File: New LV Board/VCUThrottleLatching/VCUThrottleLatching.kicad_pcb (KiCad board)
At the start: 2 copper layers, 42 x 41.5 mm, 9 parts, among them J1 B12B-PH-K-S:JST_B12B-PH-K-S, U1 IRLML2060TRPBF, U2 IRLML2060TRPBF

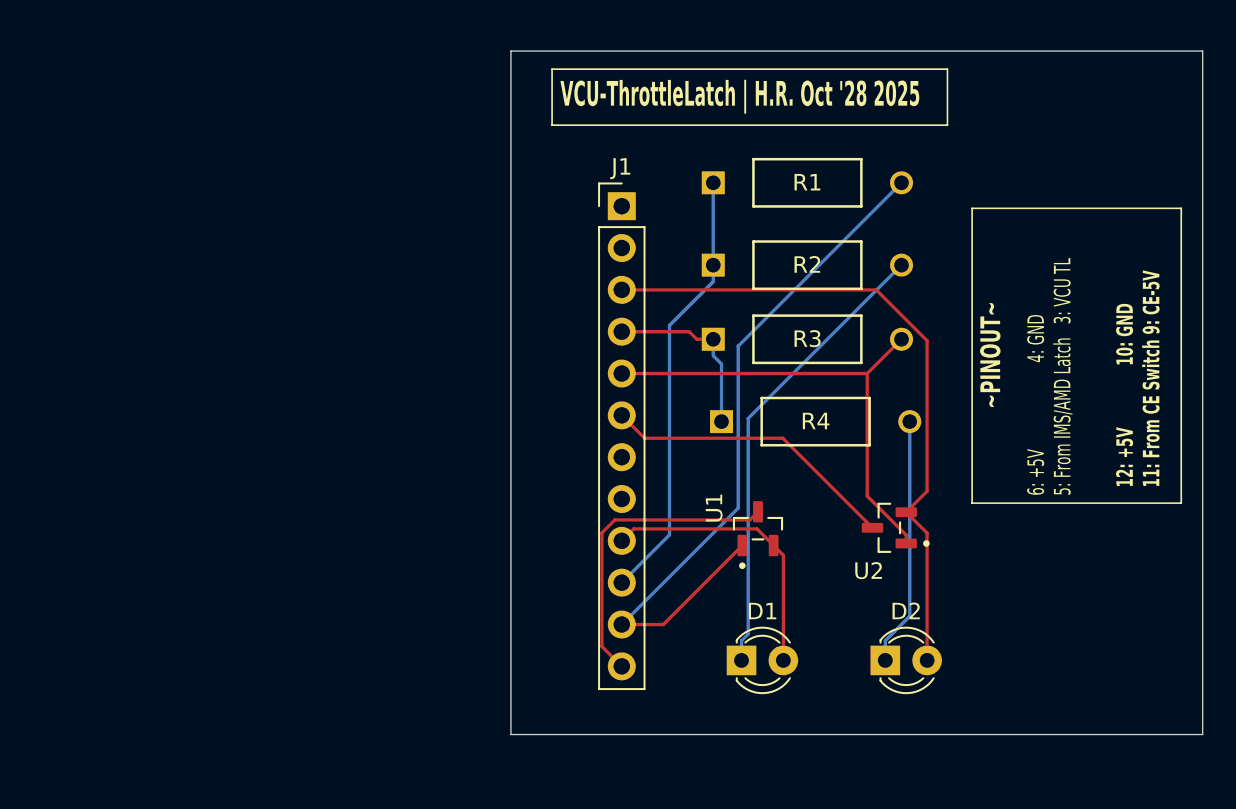
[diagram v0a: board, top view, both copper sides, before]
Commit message: Precharge added to VCU Throttle Latching
Precharge Module
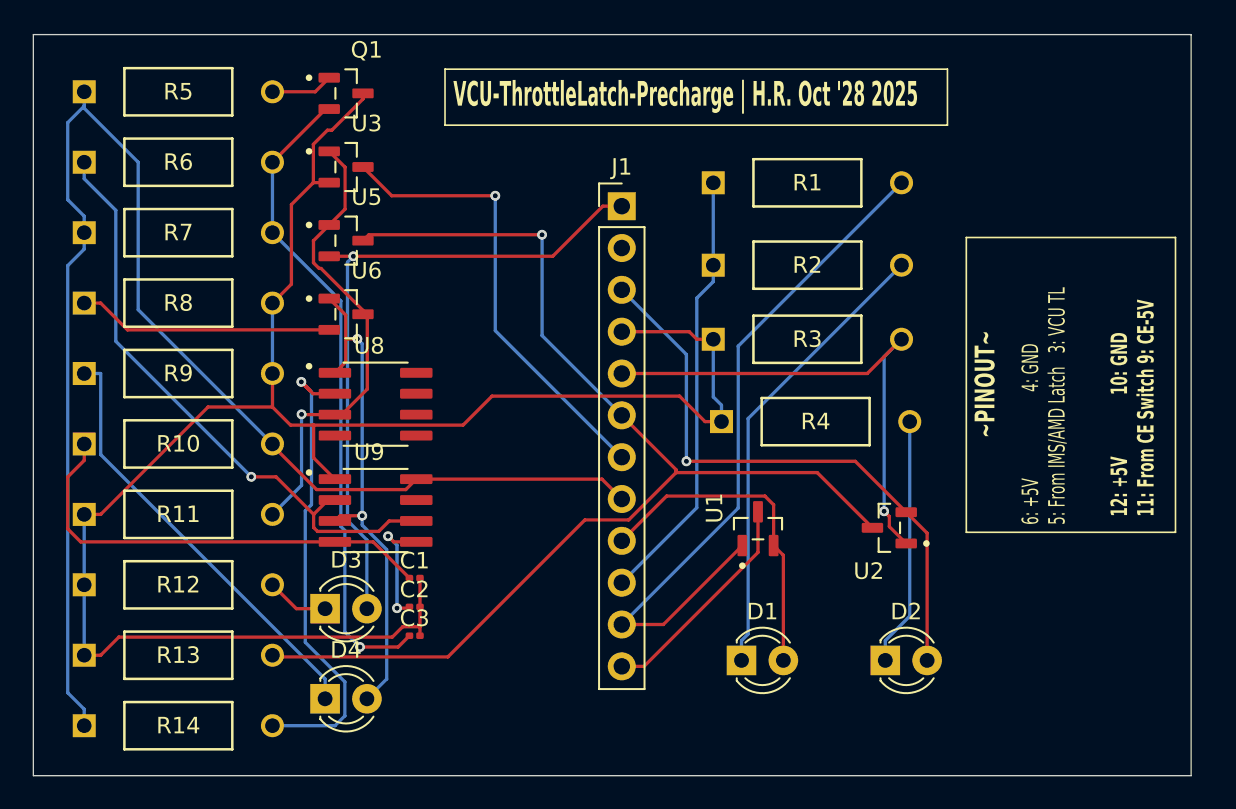
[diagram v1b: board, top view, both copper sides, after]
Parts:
- added C1: 0.1u, Capacitor_SMD:C_0201_0603Metric, F.Cu at (105.7, 104.0)
- added C2: 0.1u, Capacitor_SMD:C_0201_0603Metric, F.Cu at (105.7, 105.8)
- added C3: 47u, Capacitor_SMD:C_0201_0603Metric, F.Cu at (105.7, 107.5)
- added D3: LED (Test), LED_THT:LED_D3.0mm, F.Cu at (100.2, 105.9)
- added D4: 3 second timer, LED_THT:LED_D3.0mm, F.Cu at (100.2, 111.3)
- added Q1: SS8550, Footprints:SOT95P237X112-3N, F.Cu at (101.5, 74.6)
- added R10: 22k, Footprints:STA_CF14_STP, F.Cu at (85.6, 95.9)
- added R11: 10k, Footprints:STA_CF14_STP, F.Cu at (85.6, 100.1)
- added R12: 150R, Footprints:STA_CF14_STP, F.Cu at (85.6, 104.4)
- added R13: 10k, Footprints:STA_CF14_STP, F.Cu at (85.6, 108.7)
- added R14: 2k, Footprints:STA_CF14_STP, F.Cu at (85.6, 113.0)
- added R5: 1k, Footprints:STA_CF14_STP, F.Cu at (85.6, 74.5)
- added R6: 1k, Footprints:STA_CF14_STP, F.Cu at (85.6, 78.7)
- added R7: 57.6k, Footprints:STA_CF14_STP, F.Cu at (85.6, 83.0)
- added R8: 500, Footprints:STA_CF14_STP, F.Cu at (85.6, 87.3)
- added R9: 1k, Footprints:STA_CF14_STP, F.Cu at (85.6, 91.6)
- added U3: IRLML2060TRPBF, Footprints:SOT95P237X112-3N, F.Cu at (101.5, 79.0)
- added U5: IRLML2060TRPBF, Footprints:SOT95P237X112-3N, F.Cu at (101.5, 83.5)
- added U6: IRLML2060TRPBF, Footprints:SOT95P237X112-3N, F.Cu at (101.5, 88.0)
- added U8: PMV160UP, Footprints:SOIC127P599X175-8N, F.Cu at (103.3, 93.4)
- added U9: NE555D, Footprints:SOIC127P599X175-8N, F.Cu at (103.3, 99.9)
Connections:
- J1 pad 1: unconnected-(J1-Pad1) -> Net-(D3-A)
- J1 pad 7: unconnected-(J1-Pad7) -> Net-(U3-D)
- J1 pad 8: unconnected-(J1-Pad8) -> Net-(U9-VCC)
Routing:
- net Net-(Q1-C): track 11.0 -> 113.6 mm
- net Net-(U9-VCC): track 0.00 -> 88.6 mm
- net Net-(U2-D): track 18.0 -> 71.3 mm, vias 0 -> 1
- net Net-(D3-A): track 0.00 -> 41.1 mm, vias 0 -> 1
- net Net-(Q1-E): track 0.00 -> 39.7 mm, vias 0 -> 1
- net Net-(U9-THR): track 0.00 -> 37.1 mm, vias 0 -> 1
- net Net-(R14-Pad2): track 0.00 -> 31.7 mm, vias 0 -> 1
- net Net-(D4-A): track 0.00 -> 30.8 mm, vias 0 -> 2
- net Net-(U3-G): track 0.00 -> 28.6 mm, vias 0 -> 1
- net Net-(U3-D): track 0.00 -> 27.8 mm, vias 0 -> 1
- net Net-(U9-R): track 0.00 -> 27.6 mm
- net Net-(D4-K): track 0.00 -> 26.4 mm
- net Net-(U6-S): track 0.00 -> 15.6 mm
- net Net-(U9-CV): track 0.00 -> 7.61 mm, vias 0 -> 2
- net Net-(U1-D): track 18.6 -> 13.6 mm
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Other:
- board size 42 x 41.5 mm -> 70.3 x 45 mm
- board text added: "VCU-ThrottleLatch-Precharge | H.R. Oct '28 2025"
- board text removed: "VCU-ThrottleLatch | H.R. Oct '28 2025"
